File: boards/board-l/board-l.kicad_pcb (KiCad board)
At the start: 0 parts

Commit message: fix(board-l): resolve PCB DRC violations
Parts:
- added C10: 10uF/50V, zudo-led-lamp:C1206, F.Cu at (47.8, 52.5)
- added C11: 10uF/50V, zudo-led-lamp:C1206, F.Cu at (47.8, 54.8)
- added C12: 10uF/50V, zudo-led-lamp:C1206, F.Cu at (49.8, 57.2)
- added C13: 100nF/50V, zudo-led-lamp:C0603, F.Cu at (45.0, 57.8)
- added C14: 10uF/50V, zudo-led-lamp:C1206, F.Cu at (56.2, 43.8)
- added C15: 100nF/50V, zudo-led-lamp:C0603, F.Cu at (39.8, 53.4)
- added C16: 22uF/25V, zudo-led-lamp:C0805, F.Cu at (27.2, 40.5)
- added C17: 22uF/25V, zudo-led-lamp:C0805, F.Cu at (27.2, 42.5)
- added C18: 100nF/50V, zudo-led-lamp:C0603, F.Cu at (55.6, 33.5)
- added C19: 1uF/50V, zudo-led-lamp:C0603, F.Cu at (55.6, 30.8)
- added C20: 100nF/50V, zudo-led-lamp:C0603, F.Cu at (36.3, 53.6)
- added C21: 100nF/50V, zudo-led-lamp:C0603, F.Cu at (19.5, 49.5)
- added C22: 100nF/50V, zudo-led-lamp:C0603, F.Cu at (36.3, 51.0)
- added C23: 100nF/50V, zudo-led-lamp:C0603, F.Cu at (35.9, 45.8)
- added C24: 100nF/50V, zudo-led-lamp:C0603, F.Cu at (31.0, 27.0)
- added D10: SMAJ20A, zudo-led-lamp:SMA_L4.2-W2.6-LS5.3-RD, F.Cu at (54.2, 38.8)
- added D11: SS26, zudo-led-lamp:SMA_L4.3-W2.6-LS5.0-FD, F.Cu at (10.8, 57.8)
- added F1: PPTC 750mA/30V, zudo-led-lamp:F1206, F.Cu at (42.0, 56.4)
- added J2: 2.54mm 1x6 female, zudo-led-lamp:HDR-TH_6P-P2.54-V-F, B.Cu at (29.4, 37.7)
- added J3: SWD 1x5 (hand-fit), zudo-led-lamp:HDR-TH_5P-P2.54-V-M, B.Cu at (58.0, 29.5)
- added J4: UART pads, zudo-led-lamp:PogoPad_1x03_P2.54mm, F.Cu at (30.0, 58.2)
- added L1: 33uH, zudo-led-lamp:IND-SMD_L7.0-W6.6_FXL0630, F.Cu at (10.5, 40.3)
- added L2: 4.7uH, zudo-led-lamp:IND-SMD_L4.0-W4.0_FNR40XXS, F.Cu at (32.2, 42.8)
- added LED1: 2835 3000K CRI80, zudo-led-lamp:LED-SMD_L3.3-W2.8-RD, F.Cu at (46.2, 48.7)
- added LED10: 2835 3000K CRI80, zudo-led-lamp:LED-SMD_L3.3-W2.8-RD, F.Cu at (6.96, 8.72)
- added LED11: 2835 3000K CRI80, zudo-led-lamp:LED-SMD_L3.3-W2.8-RD, F.Cu at (10.4, 8.72)
- added LED12: 2835 3000K CRI80, zudo-led-lamp:LED-SMD_L3.3-W2.8-RD, F.Cu at (14.5, 8.72)
- added LED13: 2835 3000K CRI80, zudo-led-lamp:LED-SMD_L3.3-W2.8-RD, F.Cu at (39.2, 22.9)
- added LED14: 2835 3000K CRI80, zudo-led-lamp:LED-SMD_L3.3-W2.8-RD, F.Cu at (43.2, 22.9)
- added LED15: 2835 3000K CRI80, zudo-led-lamp:LED-SMD_L3.3-W2.8-RD, F.Cu at (47.3, 22.9)
- added LED16: 2835 3000K CRI80, zudo-led-lamp:LED-SMD_L3.3-W2.8-RD, F.Cu at (13.7, 22.7)
- added LED17: 2835 3000K CRI80, zudo-led-lamp:LED-SMD_L3.3-W2.8-RD, F.Cu at (17.8, 22.7)
- added LED18: 2835 3000K CRI80, zudo-led-lamp:LED-SMD_L3.3-W2.8-RD, F.Cu at (21.8, 22.7)
- added LED19: 2835 3000K CRI80, zudo-led-lamp:LED-SMD_L3.3-W2.8-RD, F.Cu at (6.19, 48.7)
- added LED2: 2835 3000K CRI80, zudo-led-lamp:LED-SMD_L3.3-W2.8-RD, F.Cu at (50.2, 48.7)
- added LED20: 2835 3000K CRI80, zudo-led-lamp:LED-SMD_L3.3-W2.8-RD, F.Cu at (10.2, 48.7)
- added LED21: 2835 3000K CRI80, zudo-led-lamp:LED-SMD_L3.3-W2.8-RD, F.Cu at (14.3, 48.7)
- added LED22: 2835 3000K CRI80, zudo-led-lamp:LED-SMD_L3.3-W2.8-RD, F.Cu at (13.2, 31.9)
- added LED23: 2835 3000K CRI80, zudo-led-lamp:LED-SMD_L3.3-W2.8-RD, F.Cu at (17.2, 31.9)
- added LED24: 2835 3000K CRI80, zudo-led-lamp:LED-SMD_L3.3-W2.8-RD, F.Cu at (21.3, 31.9)
- added LED3: 2835 3000K CRI80, zudo-led-lamp:LED-SMD_L3.3-W2.8-RD, F.Cu at (54.3, 48.7)
- added LED4: 2835 3000K CRI80, zudo-led-lamp:LED-SMD_L3.3-W2.8-RD, F.Cu at (46.0, 8.09)
- added LED5: 2835 3000K CRI80, zudo-led-lamp:LED-SMD_L3.3-W2.8-RD, F.Cu at (50.0, 8.09)
- added LED6: 2835 3000K CRI80, zudo-led-lamp:LED-SMD_L3.3-W2.8-RD, F.Cu at (54.1, 8.09)
- added LED7: 2835 3000K CRI80, zudo-led-lamp:LED-SMD_L3.3-W2.8-RD, F.Cu at (39.2, 31.5)
- added LED8: 2835 3000K CRI80, zudo-led-lamp:LED-SMD_L3.3-W2.8-RD, F.Cu at (43.3, 31.5)
- added LED9: 2835 3000K CRI80, zudo-led-lamp:LED-SMD_L3.3-W2.8-RD, F.Cu at (47.4, 31.5)
- added R20: 10k, zudo-led-lamp:R0805, F.Cu at (23.3, 53.2)
- added R21: 33k, zudo-led-lamp:R0603, F.Cu at (17.3, 49.2)
- added R22: 10k, zudo-led-lamp:R0805, F.Cu at (19.6, 39.6)
- added R23: 10k, zudo-led-lamp:R0805, F.Cu at (30.5, 47.4)
- added R24: 10k, zudo-led-lamp:R0805, F.Cu at (23.3, 50.8)
- added R25: 10k, zudo-led-lamp:R0805, F.Cu at (30.9, 39.7)
- added R26: 100k, zudo-led-lamp:R0603, F.Cu at (36.0, 56.5)
- added R27: 100R, zudo-led-lamp:R0603, F.Cu at (22.8, 58.0)
- added R28: 100R, zudo-led-lamp:R0603, F.Cu at (36.3, 48.6)
- added R30: 33R 1% 1W, zudo-led-lamp:R2512, F.Cu at (50.3, 44.5)
- added R31: 33R 1% 1W, zudo-led-lamp:R2512, F.Cu at (43.2, 13.2)
- added R32: 33R 1% 1W, zudo-led-lamp:R2512, F.Cu at (52.0, 28.2)
- added R33: 33R 1% 1W, zudo-led-lamp:R2512, F.Cu at (11.2, 14.5)
- added R34: 33R 1% 1W, zudo-led-lamp:R2512, F.Cu at (43.5, 18.0)
- added R35: 33R 1% 1W, zudo-led-lamp:R2512, F.Cu at (4.50, 23.2)
- added R36: 33R 1% 1W, zudo-led-lamp:R2512, F.Cu at (3.00, 42.3)
- added R37: 33R 1% 1W, zudo-led-lamp:R2512, F.Cu at (4.50, 32.2)
- added REF**: MountingHole_3.2mm_M3, MountingHole:MountingHole_3.2mm_M3, F.Cu at (4.00, 4.00)
- added REF**: MountingHole_3.2mm_M3, MountingHole:MountingHole_3.2mm_M3, F.Cu at (4.00, 56.0)
- added REF**: MountingHole_3.2mm_M3, MountingHole:MountingHole_3.2mm_M3, F.Cu at (39.5, 4.00)
- added REF**: MountingHole_3.2mm_M3, MountingHole:MountingHole_3.2mm_M3, F.Cu at (20.5, 4.00)
- added REF**: MountingHole_3.2mm_M3, MountingHole:MountingHole_3.2mm_M3, F.Cu at (56.0, 56.0)
- added RS1: 200mR 1% 2W, zudo-led-lamp:R2512, F.Cu at (19.6, 42.9)
- added RT1: NTC 10k B3380, zudo-led-lamp:R0603, F.Cu at (31.0, 28.2)
- added SW1: EC11 15-detent, zudo-led-lamp:SW-TH_ALPS_EC11L1525G01, F.Cu at (30.1, 11.1)
- added TP1: CTRL test pad, zudo-led-lamp:TestPad_D1.5mm, F.Cu at (21.0, 58.4)
- added U2: AL8860MP-13, zudo-led-lamp:MSOP-8_L3.0-W3.0-P0.65-LS4.9-BL-EP1.8, F.Cu at (18.8, 55.3)
- added U3: STM32G031F8P6, zudo-led-lamp:TSSOP-20_L6.5-W4.4-P0.65-LS6.4-BL, F.Cu at (30.1, 53.2)
- added U4: AP63203WU-7, zudo-led-lamp:TSOT-26_L2.9-W1.6-P0.95-LS2.8-BL, F.Cu at (39.2, 57.2)
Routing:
- net LED_P: track 0.00 -> 167.0 mm
- net LED_N: track 0.00 -> 162.6 mm, vias 0 -> 2
- net V15: track 0.00 -> 119.4 mm, vias 0 -> 4
- net GND: track 0.00 -> 109.4 mm, vias 0 -> 22
- net V3P3: track 0.00 -> 100.4 mm, vias 0 -> 2
- net SWDIO: track 0.00 -> 63.7 mm, vias 0 -> 3
- net ENC_A_SW: track 0.00 -> 60.7 mm, vias 0 -> 1
- net NTC_SENSE: track 0.00 -> 57.1 mm, vias 0 -> 4
- net SWCLK: track 0.00 -> 54.0 mm, vias 0 -> 3
- net ENC_A: track 0.00 -> 38.9 mm, vias 0 -> 3
- net ENC_B_SW: track 0.00 -> 38.6 mm, vias 0 -> 1
- net NRST: track 0.00 -> 37.6 mm, vias 0 -> 1
- net ATT: track 0.00 -> 28.8 mm, vias 0 -> 1
- net VBUS_L: track 0.00 -> 24.2 mm
- net PDOK: track 0.00 -> 20.7 mm, vias 0 -> 1
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- added copper zone on B.Cu, net GND
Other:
- board outline added: 60 x 60 mm
- copper layers 0 -> 2

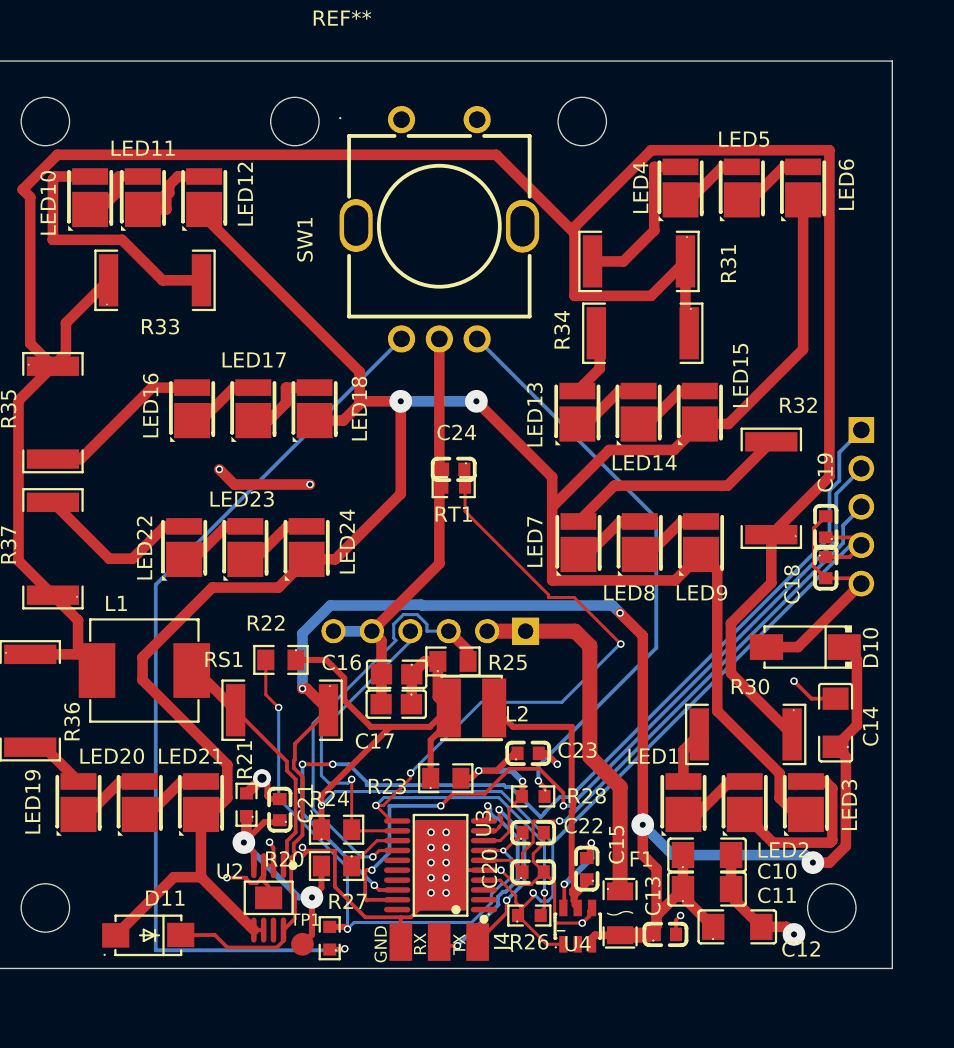
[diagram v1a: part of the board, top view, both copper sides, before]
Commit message: Route rear controls clear of the pillar-mounted power board
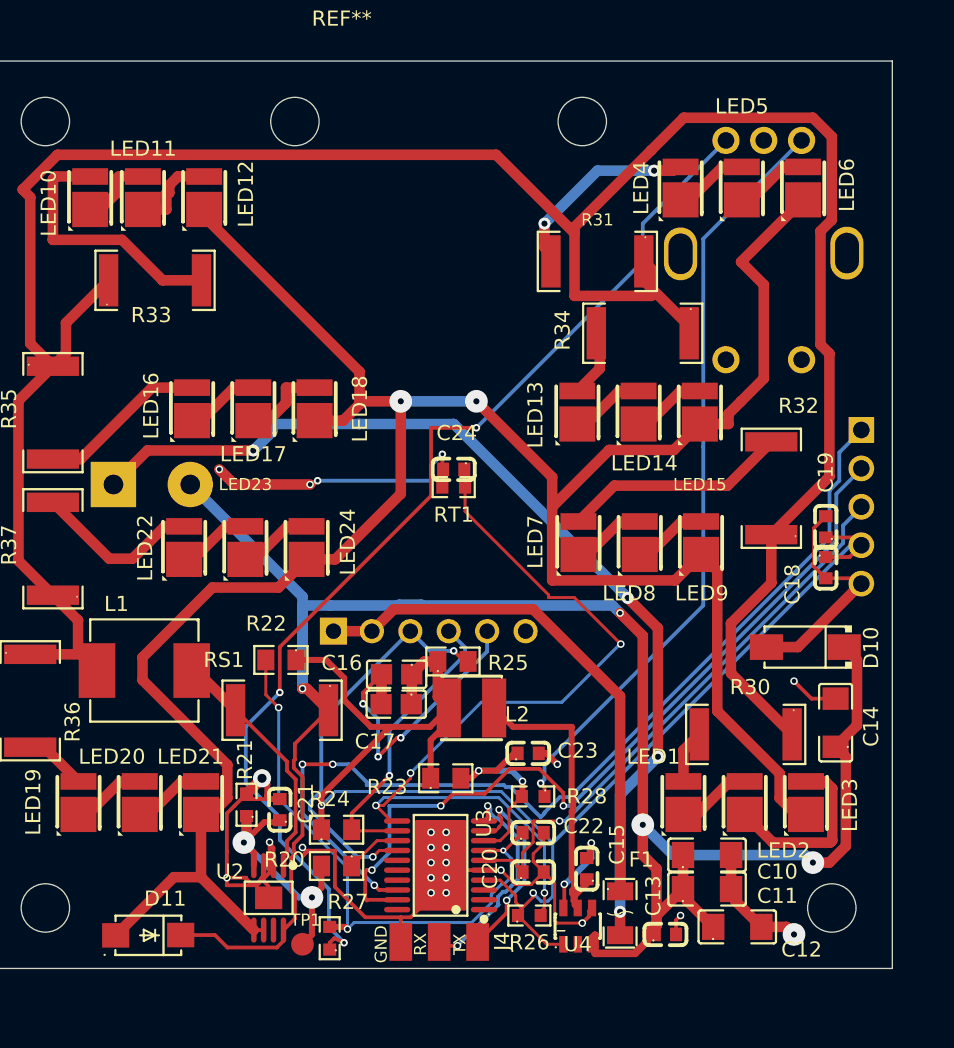
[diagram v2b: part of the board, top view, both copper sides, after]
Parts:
- added J5: Power switch solder pads, zudo-led-lamp:SolderWire_1x02_P5.08mm, B.Cu at (8.50, 28.0)
- SW1: moved to B.Cu
- moved SW1 21.5 mm to (51.5, 12.5)
- moved R31 2.75 mm to (40.5, 13.2)
- turned J2 to 0 degrees
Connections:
- F1 pad 2: V15 -> V15_FUSED
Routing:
- net V15_FUSED: track 0.00 -> 64.9 mm, vias 0 -> 4
- net V15: track 119.4 -> 137.2 mm
- net GND: track 109.4 -> 125.9 mm, vias 22 -> 27
- net ENC_B_SW: track 38.6 -> 50.6 mm
- net ENC_A_SW: track 60.7 -> 72.2 mm, vias 1 -> 3
- net VBUS_L: track 24.2 -> 34.8 mm
- net LED_P: track 167.0 -> 170.4 mm
- net LED_S2_A: track 10.9 -> 13.4 mm, vias 0 -> 2
- net ATT: track 28.8 -> 26.4 mm, vias 1 -> 2
- net LED_N: track 162.6 -> 163.9 mm
- net PDOK: track 20.7 -> 19.7 mm
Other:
- board text added: "BOARD P REAR ENVELOPE"

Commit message: Place and route rear C496154 switch clear of the stacked power board
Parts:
- removed J5: Power switch solder pads, zudo-led-lamp:SolderWire_1x02_P5.08mm
- added SW2: Power ON/OFF toggle, zudo-led-lamp:SW-TH_1MS1T1B1M1QES-5, B.Cu at (9.10, 27.8)
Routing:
- net LED_S8_A: track 11.1 -> 18.6 mm, vias 0 -> 2
- net V15: track 137.2 -> 144.0 mm
- net LED_S6_A: track 11.2 -> 14.8 mm

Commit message: Replace tall bottom controls with short slider and ALPS potentiometer (#115)
* feat: replace tall controls with stopped ALPS pot and short slider

* feat: route low-profile controls and audit assembly geometry

* docs: publish ALPS potentiometer and slider evidence and previews

* docs: fix rear-controls brightness section link
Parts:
- removed C23: 100nF/50V, zudo-led-lamp:C0603
- removed R23: 10k, zudo-led-lamp:R0805
- removed R28: 100R, zudo-led-lamp:R0603
- removed SW1: EC11 15-detent, zudo-led-lamp:SW-TH_ALPS_EC11L1525G01
- added RV1: 10k brightness pot, zudo-led-lamp:POT-TH_RK10J11E0034, B.Cu at (51.9, 9.50)
- R22: value 10k -> 100k wiper pull-down; footprint zudo-led-lamp:R0805 -> zudo-led-lamp:R0603
- SW2: value Power ON/OFF toggle -> Power ON/OFF slide; footprint zudo-led-lamp:SW-TH_1MS1T1B1M1QES-5 -> zudo-led-lamp:SW-TH_SS-12D01-G020
- turned SW2 to 90 degrees
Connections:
- C22 pad 1: ENC_A -> BRIGHT_ADC
- R22 pad 1: V3P3 -> BRIGHT_ADC
- R22 pad 2: ENC_A -> GND
- R27 pad 1: ENC_A_SW -> BRIGHT_WIPER
- R27 pad 2: ENC_A -> BRIGHT_ADC
- U3 pad 7: ENC_A -> BRIGHT_ADC
- U3 pad 8: ENC_B -> unconnected-(U3-PA1-Pad8)
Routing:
- net BRIGHT_ADC: track 0.00 -> 100.5 mm, vias 0 -> 6
- net ENC_A_SW: track 72.2 -> 0.00 mm, vias 3 -> 0
- net BRIGHT_WIPER: track 0.00 -> 69.2 mm, vias 0 -> 3
- net ENC_B_SW: track 50.6 -> 0.00 mm, vias 1 -> 0
- net GND: track 125.9 -> 170.6 mm
- net ENC_A: track 38.9 -> 0.00 mm, vias 3 -> 0
- net V3P3: track 100.4 -> 116.4 mm, vias 2 -> 3
- net ENC_B: track 13.2 -> 0.00 mm, vias 2 -> 0
- net LED_P: track 170.4 -> 174.3 mm
- net V15: track 144.0 -> 141.2 mm
